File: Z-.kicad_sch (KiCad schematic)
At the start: 27 parts, among them J1 200528-0100, J2 U.FL, J3 U.FL, J5 Conn_01x02, U3 USBLC6-2P6

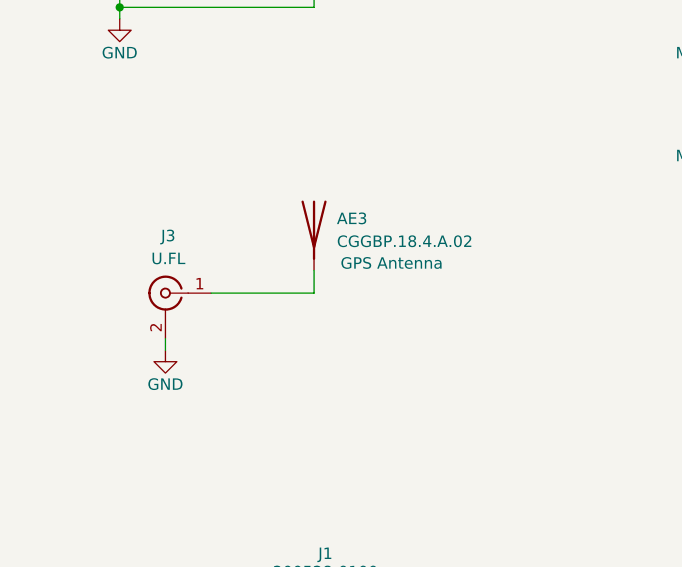
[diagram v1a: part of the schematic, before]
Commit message: Updated silkscreen and gps/antenna parameters for 50ohm
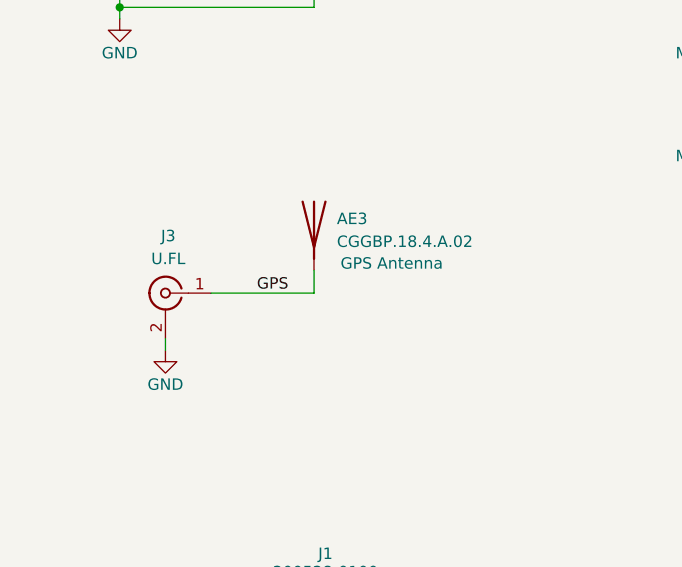
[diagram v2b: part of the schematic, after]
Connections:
- net GPS: now reaches AE3.1 (A), J3.1 (In)
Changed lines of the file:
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@@
+		)
+	)
+	(label "GPS"
+		(at 50.8 73.66 0)
+		(effects
+			(font
+				(size 1.27 1.27)
+			)
+			(justify left bottom)
 		)
 	)
